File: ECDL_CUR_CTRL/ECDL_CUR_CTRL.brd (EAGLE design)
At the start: 94 x 94 mm, 91 parts, among them IC1 LM317MDT, IC2 LM399H, IC3 OPA2227D, Q1 IRF9Z14, U1 INA213AIDCKT, U2 AD8671ARZ, U3 DMG3415U-7

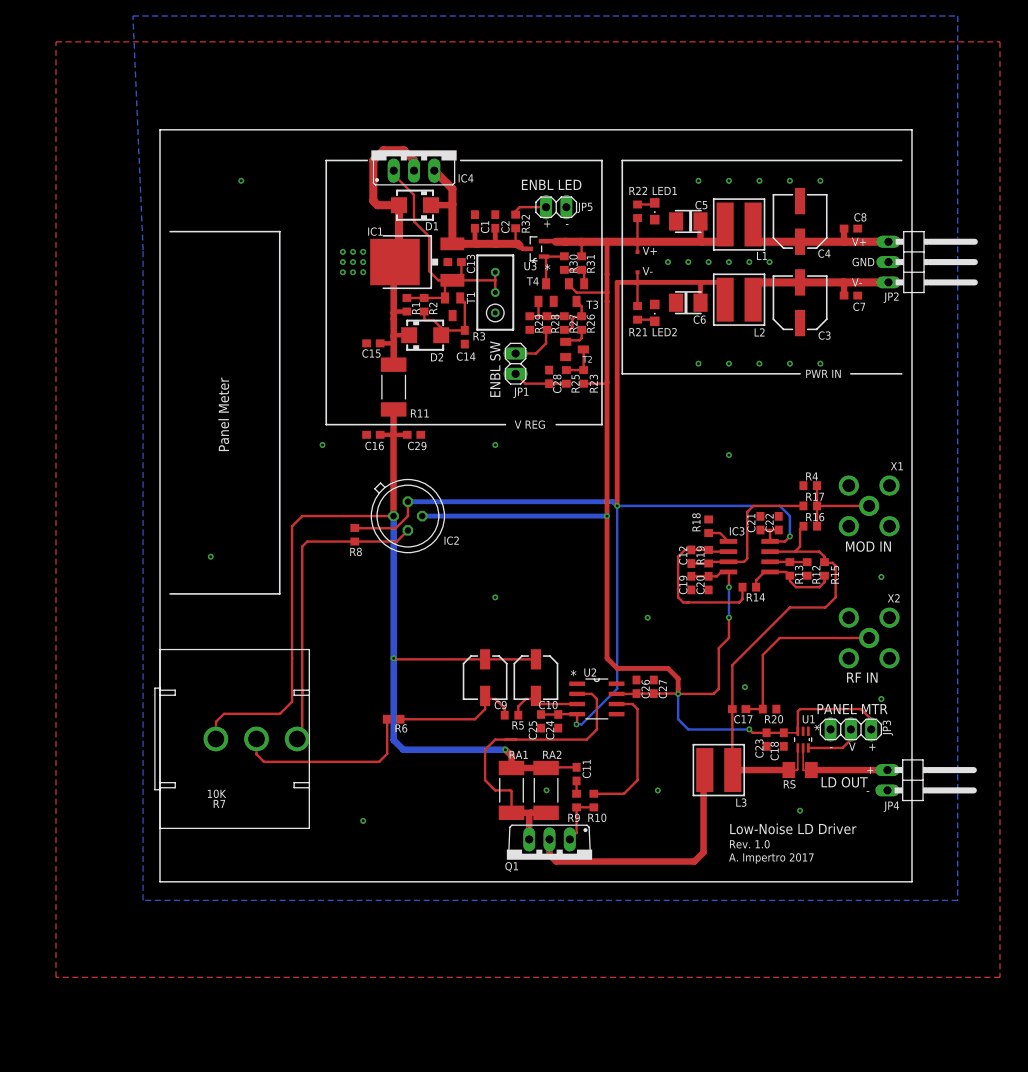
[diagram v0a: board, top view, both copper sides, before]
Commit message: Preliminary changes to new version.
New features: Microntroller for current driver as well, seperate A/D
grounding, upgrade to ARM Cortec uC, several other improvements.
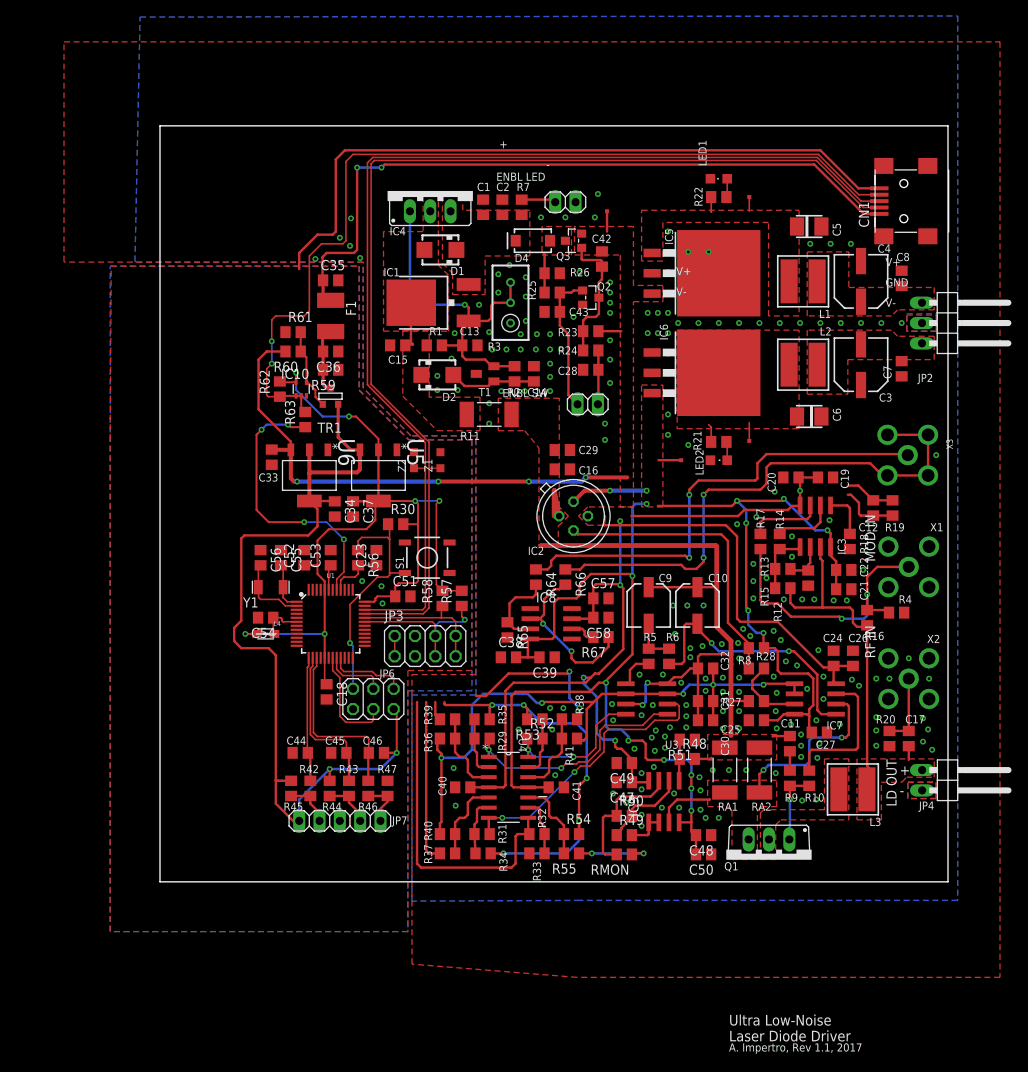
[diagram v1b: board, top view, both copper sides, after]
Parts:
- removed RS: 0.02R, adafruit:M1206
- removed T2, T3, T4: (no value), transistor:SOT23-BEC
- removed U2: AD8671ARZ, Analog Devices_By_element14_Batch_1:SOIC127P600X175-8N
- added C30, C33, C34, C36, C37, C39, C47, C48, C57: 10uF, rcl:C0805
- added C31, C32, C38, C40, C41, C44, C45, C46, C49, C50, C51, C52, C54, C55, C56, C58: 100nF, rcl:C0805
- added C35: 10nF, rcl:C0805
- added C42, C43: 0.1uF, rcl:C0805
- added C53: 1uF, rcl:C0805
- added CN1: (no value), adafruit:USB-MINIB
- added D4: 3A/40V/500mV, SparkFun-DiscreteSemi:SMA-DIODE
- added F1: MF-MSMF050-2 500mA, Arduino-M0-V1:PROTEZIONE_L1812
- added IC10: 74LVC1G125DCKR, Arduino-M0-V1:INTEGRATEDCIRCUITS_SC70-5
- added IC5: LM340S-12, linear:TO263-3
- added IC6: L7912, misc-ics:TO223-3
- added IC7, IC9: AD8676, analog-devices:SO8
- added IC8: TL071D, linear:SO08
- added JP6: (no value), pinhead:2X03
- added JP7: (no value), pinhead:1X05
- added L4: MH2029-300Y, Arduino-M0-V1:PROTEZIONE_0805
- added Q2: 2N7002, Seeed-Transistor:SOT-23
- added Q3: SSM3J328R,LF, Seeed-Transistor:SOT-23
- added R24, R47, R60, R61, R62: 100K, rcl:R0805
- added R33, R34, R35, R36, R37, R38, R39, R40, R41, R42, R43, R44, R45, R46, R48, R49, R50, R51, R52, R53, R54, R55, R57, R58, R59, R64, R65, R66, R67: 10K, rcl:R0805
- added R56, R63: 330R, rcl:R0805
- added RMON: 50R, rcl:R0805
- added S1: MOM SWITCH, SparkFun-Switches:TACTILE_SWITCH_SMD_5.2MM
- added TP3, TP4: (no value), SparkFun-Connectors:PAD.02X.02
- added TR1: PMV48XP, Arduino-M0-V1:TRANSISTORS_SOT-23
- added U4: TS514AID, ST Microelctronics_By_element14_Batch_1:SOIC127P600X175-14N
- added U5: LM1117IMP-3.3, NSC_By_element14_Batch_1.1:SOT230P696X180-4N
- added U6: LM1117IMP-5.0, NSC_By_element14_Batch_1.1:SOT230P696X180-4N
- added X3: (no value), adafruit:SMA90_DIP
- added Y1: 32,768Khz_SMD, Arduino-M0-V1:CRISTALLI_RESONATOR_EPSON_FC_145
- added Z1, Z2: BRNCG0603MLC-05E, Arduino-M0-V1:PROTEZIONE_CT/CN0603
- C1: value 100nF -> 10nF; device rcl:C0603 -> rcl:C0805
- C11: value C_SNUB -> Cfb; device rcl:C0603 -> rcl:C0805
- C12: value 1u -> 1uF; device rcl:C0603 -> rcl:C0805
- C13, C14, C15, C16, C17, C2, C20, C21, C25, C28, C7, C8: device rcl:C0603 -> rcl:C0805
- C18, C19, C22, C26, C29: value 0.1uF -> 100nF; device rcl:C0603 -> rcl:C0805
- C23: value 10uF -> 10nF; device rcl:C0603 -> rcl:C0805
- C24: value 0.1uF -> 10uF; device rcl:C0603 -> rcl:C0805
- C27: value 10uF -> 100nF; device rcl:C0603 -> rcl:C0805
- JP3: device pinhead:1X03 -> pinhead:2X04
- R1, R10, R12, R13, R14, R15, R16, R17, R18, R19, R2, R20, R21, R22, R5, R6, R8: device rcl:R0603 -> rcl:R0805
- R23, R25, R26, R29: value 470K -> 10K; device rcl:R0603 -> rcl:R0805
- R27: value 10K -> 28.7K; device rcl:R0603 -> rcl:R0805
- R28: value 1K -> 11K; device rcl:R0603 -> rcl:R0805
- R30: value 100K -> 10K; device rcl:R0603 -> rcl:R0805
- R31: value 1M -> 10K; device rcl:R0603 -> rcl:R0805
- R32: value 1K -> 10K; device rcl:R0603 -> rcl:R0805
- R4: value 50 -> 50R; device rcl:R0603 -> rcl:R0805
- R7: value 10K -> 1K; device ecdl_parts:3950 -> rcl:R0805
- R9: value R_SNUB -> 100R; device rcl:R0603 -> rcl:R0805
- U1: value INA213AIDCKT -> ATSAMD21G-A; device Texas Instruments_By_element14_Batch_1:SOT65P210X110-6N -> SparkFun-IC-Microcontroller:TQFP-48
- U3: value DMG3415U-7 -> AD5541; device Diodes_Inc_By_element14_Batch_1:SOT95P240X105-3N -> misc-ics:SOIC-8
- moved R32 76.6 mm to (47.1, 5.97), turned to 0 degrees
- moved R31 72.5 mm to (40.3, 5.97), turned to 180 degrees
- moved R7 72.2 mm to (45.2, 84.3), turned to 270 degrees
- moved U1 60.8 mm to (21.3, 32.3), turned to 0 degrees
- moved U3 57.9 mm to (60.8, 22.9), turned to 270 degrees
- moved C18 57.5 mm to (20.8, 23.7)
- moved JP3 54.2 mm to (33.1, 29.5), turned to 0 degrees
- moved C23 53.8 mm to (27.1, 40.5), turned to 90 degrees
- moved R27 53.0 mm to (74.5, 22.6), turned to 0 degrees
- moved R29 52.3 mm to (40.3, 17.9), turned to 180 degrees
- moved R8 52.2 mm to (74.5, 29.2), turned to 0 degrees
- moved R28 50.5 mm to (74.5, 26.7), turned to 180 degrees
- moved R30 38.9 mm to (29.5, 44.7), turned to 0 degrees
- moved R6 35.3 mm to (63.6, 28.2), turned to 270 degrees
- moved C24 35.3 mm to (84.2, 27.9), turned to 90 degrees
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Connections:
- removed net N$31: R26.1, R27.1, T3.C
- removed net N$4 (its old number): C17.2, IC3.3, L3.2, R15.1, R16.1, RS.1, U1.4
- removed net N$6 (its old number): R6.2, R7.S
- new net +12V: C19.1, C20.1, C24.1, C26.1, C33.1, C40.1, C42.1, C47.1, C49.1, C57.1, C58.2, IC2.3, IC3.8, IC5.3, IC7.8, IC8.7, IC9.8, Q3.2, R23.2, R60.2, TP3.P$1, U4.4, U6.3
- new net +3V3: C18.1, C37.1, C51.1, C52.1, IC10.5, JP3.1, JP3.2, L4.2, R30.2, R57.2, R58.2, R62.2, U1.17, U1.36, U1.44, U5.2, U5.4
- new net +5V: C34.1, C46.1, JP6.2, JP7.1, R44.2, R45.2, TR1.2, U5.3, U6.2, U6.4
- new net -12V: C21.1, C22.1, C25.2, C27.2, C38.2, C39.2, C41.1, C48.2, C50.2, IC2.4, IC3.4, IC6.3, IC7.4, IC8.4, IC9.4, R8.2, TP4.P$1, U4.11
- new net CS: R41.1
- new net DACGND: C30.2, C31.2, C32.2, IC7.1, IC7.2, R36.2, R37.2, R38.2, U3.2, U3.7
- new net DCLK: R29.1, U3.5, U4.1
- new net DCS: R52.1, U3.4, U4.14
- new net DCURMON: R32.1, U4.8
- new net DDATA: R31.1, U3.6, U4.7
- new net DGND: C18.2, C23.2, C33.2, C34.2, C35.2, C36.1, C37.2, C44.2, C45.2, C51.2, C52.2, C53.2, C54.2, C55.1, C56.1, CN1.GND, IC10.3, JP3.3, JP3.4, JP6.6, JP7.3, R34.2, R35.2, R47.1, R53.2, R54.2, R59.1, R61.1, R65.2, S1.1, U1.18, U1.35, U1.42, U1.5, U5.1, U6.1, Z1.2, Z2.2
- new net ENCA: C45.1, R43.1, U1.14
- new net ENCB: C44.1, R42.1, U1.13
- new net ENCBTN: C46.2, R46.1, U1.15
- new net MOSI: R40.1
- new net N$29: IC7.3, R27.2, R28.1
- new net N$35: C17.1, IC3.3, JP4.1, L3.2, R15.2, R16.1
- new net N$36: JP7.2, R42.2, R45.1
- new net N$38: IC8.3, R64.2, R65.1
- new net N$39: R32.2, R33.1, U4.9
- new net N$40: JP7.4, R43.2, R44.1
- new net N$41: R37.1, R40.2, U4.5
- new net N$42: R38.1, R41.2, U4.12
- new net N$43: JP7.5, R46.2, R47.2
- new net N$44: C55.2, U1.1, Y1.P$2
- new net N$45: C56.2, U1.2, Y1.P$1
- new net N$46: IC10.4, R60.1, R61.2, TR1.3
- new net N$47: IC8.2, R66.2, R67.1
- new net N$5: R5.1, U3.1
- new net N$50: IC9.1, IC9.2, R49.2
- new net N$51: IC9.5, R48.1, R51.2
- new net N$52: IC9.6, R49.1, R50.2
- new net N$54: IC9.7, R50.1, RMON.2
- new net N$55: R54.1, R55.2, U4.10
- new net N$56: R52.2, R53.1, U4.13
- new net N$9: IC7.7, R10.2
- new net PA02_AIN0: U1.3
- new net PA04_AIN4: U1.9
- new net PA05_AIN5: U1.10
- new net PA28_USB_HOST_EN: R63.1, U1.41
- new net PB02_AIN10: U1.47
- new net PB08_AIN2: U1.7
- new net PB09_AIN3: U1.8
- new net PB10_S4_SPI_MOSI: JP6.4, U1.19
- new net PB11_S4_SPI_SCK: JP6.3, U1.20
- new net PB12_S4_SPI_MISO: JP6.1, U1.21
- new net RESET: JP6.5, R30.1, R56.1, S1.3
- new net SCK: R39.1
- new net SCL: JP3.7, JP3.8, R58.1, U1.32
- new net SDA: JP3.5, JP3.6, R57.1, U1.31
- new net TARGET_RESET: C23.1, R56.2, U1.40
- new net TARGET_USB_N: CN1.D-, U1.33, Z1.1
- new net TARGET_USB_P: CN1.D+, U1.34, Z2.1
- new net USBVCC: C36.2, F1.2, R59.2, TR1.1
- new net USB_ID: CN1.ID, IC10.1, IC10.2, R62.1, R63.2
- new net VDDCORE: C53.1, U1.43
- new net VIN: IC8.6, R67.2
- new net VMON: R55.1, RMON.1
- new net XUSB: C35.1, CN1.VBUS, F1.1
- net GND: now also C19.2, C20.2, C25.1, C27.1, C38.1, C39.1, C40.2, C41.2, C43.2, C47.2, C48.1, C49.2, C50.1, C57.2, C58.1, IC5.TAB, IC6.1, Q2.2, R12.1, R20.1, R26.1, R33.2, R4.2, R51.1; no longer C18.2, C19.1, C20.1, C23.2, C25.2, C27.2, JP3.3, R12.2, R20.2, R29.2, R4.1, T2.E, T4.E, U1.1, U1.2
- net N$1: now also R1.2, R2.2; no longer R1.1, R2.1
- net N$10: now also R29.2, R35.1, U4.2; no longer R10.2, U2.6
- net N$12: now also C43.1, Q2.1, R25.1; no longer R28.1
- net N$13: now also IC7.6, IC9.3; no longer U2.2
- net N$15: now also R12.2; no longer R12.1
- net N$16: now also R15.1; no longer R15.2
- net N$17: now also R17.2; no longer R17.1
- net N$18: now also R17.1, R4.1; no longer R17.2, R4.2
- net N$20: now also C17.2, R20.2; no longer C17.1, R20.1
- net N$23: now also R36.1, R39.2, U4.3; no longer JP4.1, RS.2, U1.5
- net N$24: now also D4.C, R7.2; no longer R32.2, U3.3
- net N$25: now also C54.1, L4.1; no longer JP3.2
- net N$26: now also C28.1, JP1.2, R24.1; no longer R23.1, R25.2, T2.C
- net N$27: now also R1.1; no longer R1.2
- net N$28: now also C42.2, Q2.3, Q3.1, R23.1, R24.2; no longer C28.1, JP1.2, R25.1
- net N$3: now also R2.1; no longer R2.2
- net N$30: now also D4.A, Q3.3, R25.2; no longer T2.B
- net N$32: now also R31.2, R34.1, U4.6; no longer R27.2, R28.2, R29.1, T4.B
- net N$33: now also R66.1, X3.GND1, X3.GND2, X3.GND3, X3.GND4; no longer R30.2, T4.C, U3.1
- net N$34: now also R64.1, X3.ANTENNA; no longer R30.1, R31.2, T3.B
- net N$37: now also R7.1; no longer R32.1
- net N$7: now also IC7.5, R6.2; no longer R5.1, U2.3
- net N$8: now also R28.2; no longer R7.A
- net V+: now also IC5.1; no longer C18.1, C19.2, C20.2, C23.1, C26.1, C27.1, IC2.3, IC3.8, JP3.1, R23.2, R31.1, T3.E, U1.3, U2.7, U3.2
- net V-: now also IC6.TAB; no longer C21.1, C22.1, C24.1, C25.1, IC2.4, IC3.4, R8.2, U2.4
- net VCCINT: now also C30.1, C31.1, C32.1, R27.1, R48.2, U3.3, U3.8; no longer R7.E
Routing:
- net +12V: track 0.00 -> 225.4 mm, vias 0 -> 9
- net -12V: track 0.00 -> 198.0 mm, vias 0 -> 16
- net V+: track 195.8 -> 3.71 mm, vias 5 -> 0
- net V-: track 154.1 -> 4.58 mm, vias 3 -> 0
- net DGND: track 0.00 -> 138.3 mm, vias 0 -> 8
- net TARGET_USB_N: track 0.00 -> 134.4 mm
- net TARGET_USB_P: track 0.00 -> 134.2 mm
- net +3V3: track 0.00 -> 116.2 mm, vias 0 -> 6
- net USB_ID: track 0.00 -> 112.8 mm, vias 0 -> 2
- net +5V: track 0.00 -> 109.7 mm, vias 0 -> 2
- net XUSB: track 0.00 -> 89.8 mm, vias 0 -> 2
- net DACGND: track 0.00 -> 79.1 mm, vias 0 -> 5
- net N$33: track 6.06 -> 68.3 mm, vias 0 -> 2
- net N$4 (its old number): track 57.8 -> 0.00 mm
- net N$34: track 4.02 -> 59.2 mm, vias 0 -> 2
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- added copper zone on layer 1, net +12V
- added copper zone on layer 1, net +15V
- added copper zone on layer 1, net -12V
- added copper zone on layer 1, net -15V
- added copper zone on layer 1, net DGND
- added copper zone on layer 16, net DGND
- added copper zone on layer 1, net N$13
- added copper zone on layer 1, net N$2
- added copper zone on layer 1, net N$24
- added copper zone on layer 1, net N$27
- added copper zone on layer 1, net N$30
- added copper zone on layer 1, net N$35
- added copper zone on layer 1, net V+
- added copper zone on layer 1, net V-
- added copper zone on layer 1, net VCCINT
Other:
- board size 94 x 94 mm -> 98.5 x 94.5 mm
- board text added: "5V"
- board text added: "A"
- board text added: "A. Impertro, Rev 1.1, 2017"
- board text added: "B"
- board text added: "BTN"
- board text added: "Display"
- board text added: "ICSP"
- board text added: "Rotary Encoder"
- board text added: "TP1"
- board text added: "TP2"
- board text added: "Ultra Low-Noise Laser Diode Driver"
- board text removed: "A. Impertro 2017"
- board text removed: "Low-Noise LD Driver"
- board text removed: "PANEL MTR"
- board text removed: "Panel Meter"
- board text removed: "Rev. 1.0"
- board text removed: "V"

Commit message: Rev1.1 of CUR CTRL Complete, Ready for Mfg. Temp Ctrl WIP
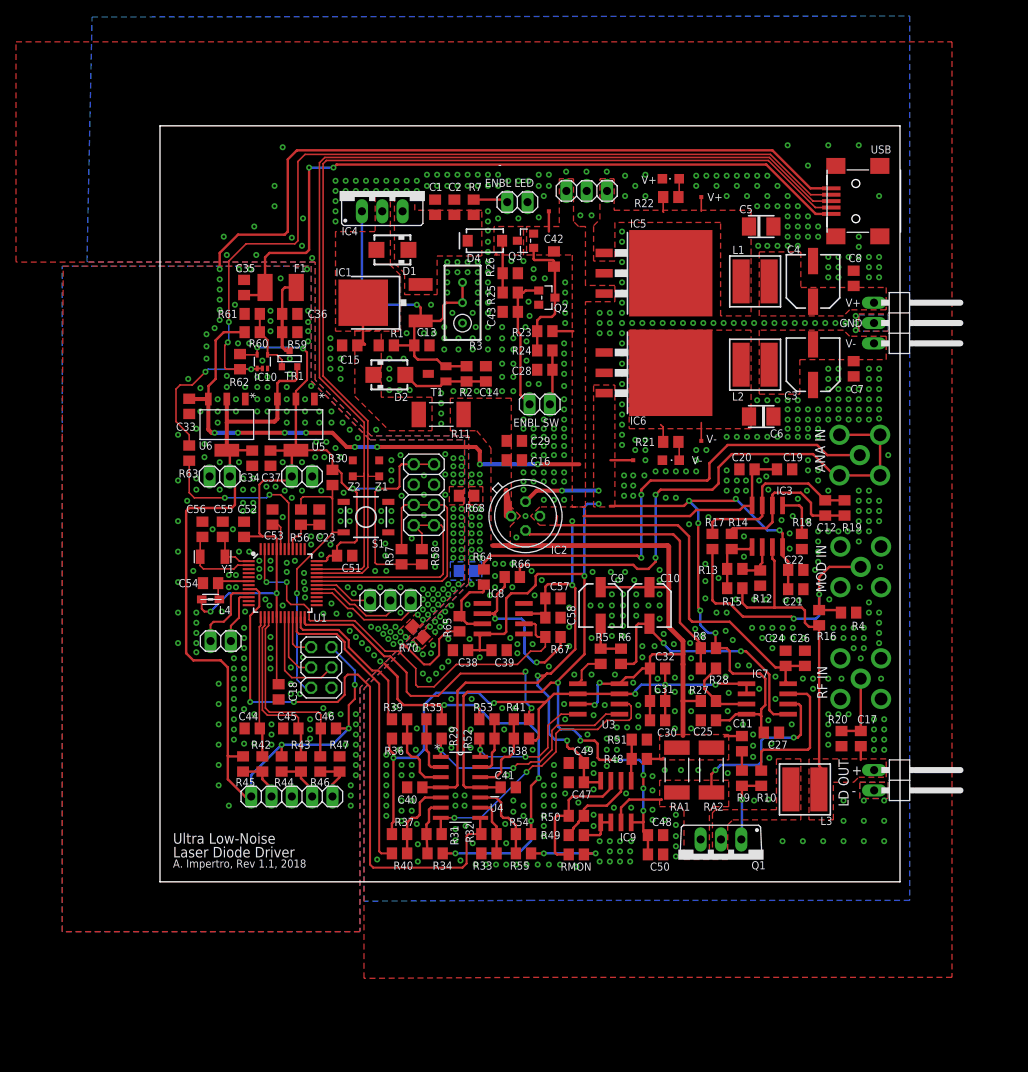
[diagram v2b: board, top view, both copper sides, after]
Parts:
- removed CN1: (no value), adafruit:USB-MINIB
- removed LED1, LED2: (no value), led:CHIPLED_0805
- added JP10, JP12: (no value), pinhead:1X03
- added JP11, JP8, JP9: (no value), pinhead:1X02
- added R68, R69, R70: 0R, rcl:R0805
- added USB: (no value), adafruit:USB-MINIB
- added V+, V-: (no value), led:CHIPLED_0805
- C11: value Cfb -> 33nF
- RMON: value 50R -> 50R or 0R
- moved JP3 18.9 mm to (33.0, 48.4), turned to 270 degrees
- moved R63 15.1 mm to (3.65, 53.6)
- moved C33 12.1 mm to (3.65, 59.4)
- moved C34 12.1 mm to (11.5, 53.0)
- moved U5 12.1 mm to (17.0, 57.1)
- moved C37 12.1 mm to (13.8, 53.0)
- moved U6 12.1 mm to (8.35, 57.1)
- moved C35 10.9 mm to (10.5, 74.3), turned to 90 degrees
- moved R30 9.83 mm to (21.6, 50.5), turned to 90 degrees
- moved S1 9.18 mm to (25.8, 45.6)
- moved R57 9.15 mm to (30.2, 40.6), turned to 270 degrees
- moved C51 8.87 mm to (23.1, 40.8)
- moved C53 8.87 mm to (14.1, 45.6)
- moved C23 8.77 mm to (19.9, 45.6)
- moved R56 8.77 mm to (17.6, 45.6)
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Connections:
- net PB08_AIN2 renamed N$31
- removed net CS: R41.1
- removed net MOSI: R40.1
- removed net PB02_AIN10: U1.47
- removed net PB09_AIN3: U1.8
- removed net SCK: R39.1
- new net CS_DAC: R41.1, U1.24
- new net MOSI_DAC: R40.1, U1.22
- new net N$48: JP10.3, U1.30
- new net N$49: JP10.2, U1.29
- new net N$53: JP10.1, U1.28
- new net SCK_DAC: R39.1, U1.23
- net +12V: now also JP12.3
- net +3V3: now also JP11.1
- net +5V: now also JP9.1
- net DCURMON: now also U1.8
- net DGND: now also JP11.2, JP9.2, R68.2, R69.2, R70.2, USB.GND; no longer CN1.GND
- net GND: now also JP12.2, R68.1, R69.1, R70.1, V+.C, V-.A; no longer LED1.C, LED2.A
- net N$21: now also V+.A; no longer LED1.A
- net N$22: now also V-.C; no longer LED2.C
- net PA04_AIN4: now also JP8.2
- net PA05_AIN5: now also JP8.1
- net TARGET_USB_N: now also USB.D-; no longer CN1.D-
- net TARGET_USB_P: now also USB.D+; no longer CN1.D+
- net USB_ID: now also USB.ID; no longer CN1.ID
- net V+: now also JP12.1
- net VIN: now also U1.47
- net XUSB: now also USB.VBUS; no longer CN1.VBUS
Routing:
- net VIN: track 3.36 -> 55.2 mm, vias 0 -> 2
- net CS_DAC: track 0.00 -> 41.2 mm, vias 0 -> 2
- net MOSI_DAC: track 0.00 -> 38.0 mm
- net DCURMON: track 40.3 -> 76.1 mm, vias 0 -> 2
- net SCK_DAC: track 0.00 -> 20.5 mm
- net MOSI: track 20.4 -> 0.00 mm
- net DGND: track 138.3 -> 158.0 mm, vias 8 -> 294
- net CS: track 19.7 -> 0.00 mm, vias 2 -> 0
- net SDA: track 20.1 -> 36.3 mm, vias 1 -> 0
- net N$53: track 0.00 -> 14.9 mm
- net USB_ID: track 112.8 -> 125.2 mm, vias 2 -> 4
- net PA28_USB_HOST_EN: track 35.3 -> 23.1 mm, vias 4 -> 2
- net N$49: track 0.00 -> 12.2 mm
- net SCL: track 17.4 -> 29.0 mm
- net +3V3: track 116.2 -> 127.3 mm
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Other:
- board size 98.5 x 94.5 mm -> 92.5 x 94.5 mm
- board text added: "+12V"
- board text added: "+3V3"
- board text added: "+5V"
- board text added: "-12V"
- board text added: "3V3"
- board text added: "A. Impertro, Rev 1.1, 2018"
- board text added: "A0"
- board text added: "ANA I/O"
- board text added: "ANA IN"
- board text added: "D0"
- board text added: "D1"
- board text added: "D2"
- board text added: "DIG I/O"
- board text added: "ENCODER"
- board text added: "HI CUR REG"
- board text added: "I2C"
- board text added: "SCL"
- board text added: "SDA"
- board text removed: "A. Impertro, Rev 1.1, 2017"
- board text removed: "Display"
- board text removed: "Rotary Encoder"
- board text removed: "TP1"
- board text removed: "TP2"
- board text removed: "V REG"

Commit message: Added a Controller for the Pfeiffer IKR/PKR Series Compact Gauges. Temp Ctrl WIP...
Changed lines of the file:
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@@
 <text x="44.165" y="56.896" size="1.016" layer="25" font="vector" ratio="12">ENBL SW</text>
 <text x="40.609" y="86.868" size="1.016" layer="25" font="vector" ratio="12">ENBL LED</text>
-<text x="42.26" y="89.154" size="1.016" layer="25" font="vector">-</text>
 <text x="86.456" y="13.335" size="1.27" layer="25" font="vector" ratio="12">+</text>
 <text x="86.456" y="10.795" size="1.27" layer="25" font="vector" ratio="12">-</text>
@@
 <text x="81.884" y="56.642" size="1.27" layer="25" font="vector" ratio="12" rot="R270">ANA IN</text>
 <text x="57.5" y="51.054" size="1.016" layer="48" font="vector" ratio="12">-12V</text>
-<text x="49.372" y="83.439" size="1.016" layer="48" font="vector" ratio="12">+12V</text>
+<text x="47.975" y="82.169" size="1.016" layer="48" font="vector" ratio="12">+12V</text>
 <text x="25.369" y="37.084" size="1.016" layer="48" font="vector" ratio="12">D0</text>
 <text x="28.036" y="37.084" size="1.016" layer="48" font="vector" ratio="12">D1</text>
@@
 <dimension x1="87.591" y1="39.37" x2="87.591" y2="25.4" x3="108.5" y3="32.385" textsize="1.778" textratio="12" layer="47" dtype="vertical"/>
 <dimension x1="87.591" y1="25.4" x2="93.076" y2="12.7" x3="108.5" y3="19.05" textsize="1.778" textratio="12" layer="47" dtype="vertical"/>
-<text x="49.022" y="88.138" size="1.016" layer="48" font="vector" ratio="12">HI CUR REG</text>
+<text x="49.149" y="83.693" size="1.016" layer="48" font="vector" ratio="12">HI CUR REG</text>
 </plain>
 <attributes>
@@
 </element>
 <element name="V+" library="led" library_urn="urn:adsk.eagle:library:259" package="CHIPLED_0805" package3d_urn="urn:adsk.eagle:package:15821/1" value="" x="63.85" y="87.884" smashed="yes" rot="R90">
-<attribute name="NAME" x="60.167" y="87.249" size="1.016" layer="25" font="vector"/>
+<attribute name="NAME" x="60.294" y="86.741" size="1.016" layer="25" font="vector"/>
 <attribute name="VALUE" x="65.12" y="90.424" size="1.27" layer="27" rot="R180"/>
 </element>
